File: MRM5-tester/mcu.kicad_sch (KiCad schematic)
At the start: 6 parts, among them U2 STM32L011F4Ux

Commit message: tester PCB 작성중
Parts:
- removed C3: 0.1u, PCM_Capacitor_SMD_AKL:C_0402_1005Metric, symbol PCM_Capacitor_AKL:C_0402
- removed C4: 1u, PCM_Capacitor_SMD_AKL:C_0402_1005Metric, symbol PCM_Capacitor_AKL:C_0402
- removed U2: STM32L011F4Ux, Package_DFN_QFN:ST_UFQFPN-20_3x3mm_P0.5mm, symbol MCU_ST_STM32L0:STM32L011F4Ux
- added D1, D2, D3, D4: LED-WHITE, LED_SMD:LED_0402_1005Metric, symbol Device:LED
- added IC1: STM32G051F8P6, Mouser:SOP65P640X120-20N, symbol ktw07182:STM32G051F8P6
- added Q1, Q2, Q3, Q4: MMBT3906-TP, Mouser:SOT95P237X125-3N, symbol ktw07182:MMBT3906-TP
- added R2, R4, R6, R8: 330, PCM_Resistor_SMD_AKL:R_0402_1005Metric, symbol PCM_Resistor_AKL:R_0402
- added R3, R5, R7: 1k, PCM_Resistor_SMD_AKL:R_0402_1005Metric, symbol PCM_Resistor_AKL:R_0402
- R1: value 10k -> 1k
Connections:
- net 1V6: now also IC1.8 (PA1)
- net GND: now also IC1.5 (VSS/VSSA), R2.2, R4.2, R6.2, R8.2; no longer R1.1
- net MCU_SW_CLK: now also IC1.19 (PA15/PA14-BOOT0)
- net MCU_SW_DIO: now also IC1.18 (PA13)
- net MCU_UART_CTS: now also IC1.16 (PA11[PA9])
- net MCU_UART_RTS: now also IC1.17 (PA12[PA10])
- net MCU_UART_RX: now also IC1.1 (PB7/PB8)
- net MCU_UART_TX: now also IC1.20 (PB3/PB4/PB5/PB6)
- net SYNC_INT: now also IC1.10 (PA3)
- net VDD: now also IC1.4 (VDD/VDDA), Q1.2 (E), Q2.2 (E), Q3.2 (E), Q4.2 (E)
- net at R1.2: now also Q1.1 (B)
- new net: D4.1 (K), R8.1
- new net: D4.2 (A), Q4.3 (C)
- new net: D2.1 (K), R4.1
- new net: D2.2 (A), Q2.3 (C)
- new net: Q2.1 (B), R3.2
- new net: Q3.1 (B), R5.2
- new net: D1.2 (A), Q1.3 (C)
- new net: D3.1 (K), R6.1
- new net: D3.2 (A), Q3.3 (C)
- new net: Q4.1 (B), R7.2
- new net: D1.1 (K), R2.1
- new net 1V6_IFlag: IC1.14 (PA7), R3.1
- new net 1V6_TFlag: IC1.15 (PB0/PB1/PB2/PA8), R1.1
- new net ADC_V: IC1.7 (PA0)
- new net DAC_Z: IC1.11 (PA4)
- new net MCU_NRST: IC1.6 (PF2-NRST)
- new net SUSPEND: IC1.3 (PC15-OSC32_OUT)
- new net WAKEUP: IC1.2 (PB9/PC14-OSC32_IN)
- new net Z_IFlag: IC1.12 (PA5), R7.1
- new net Z_TFlag: IC1.13 (PA6), R5.1
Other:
- moved on the sheet: C1, C2

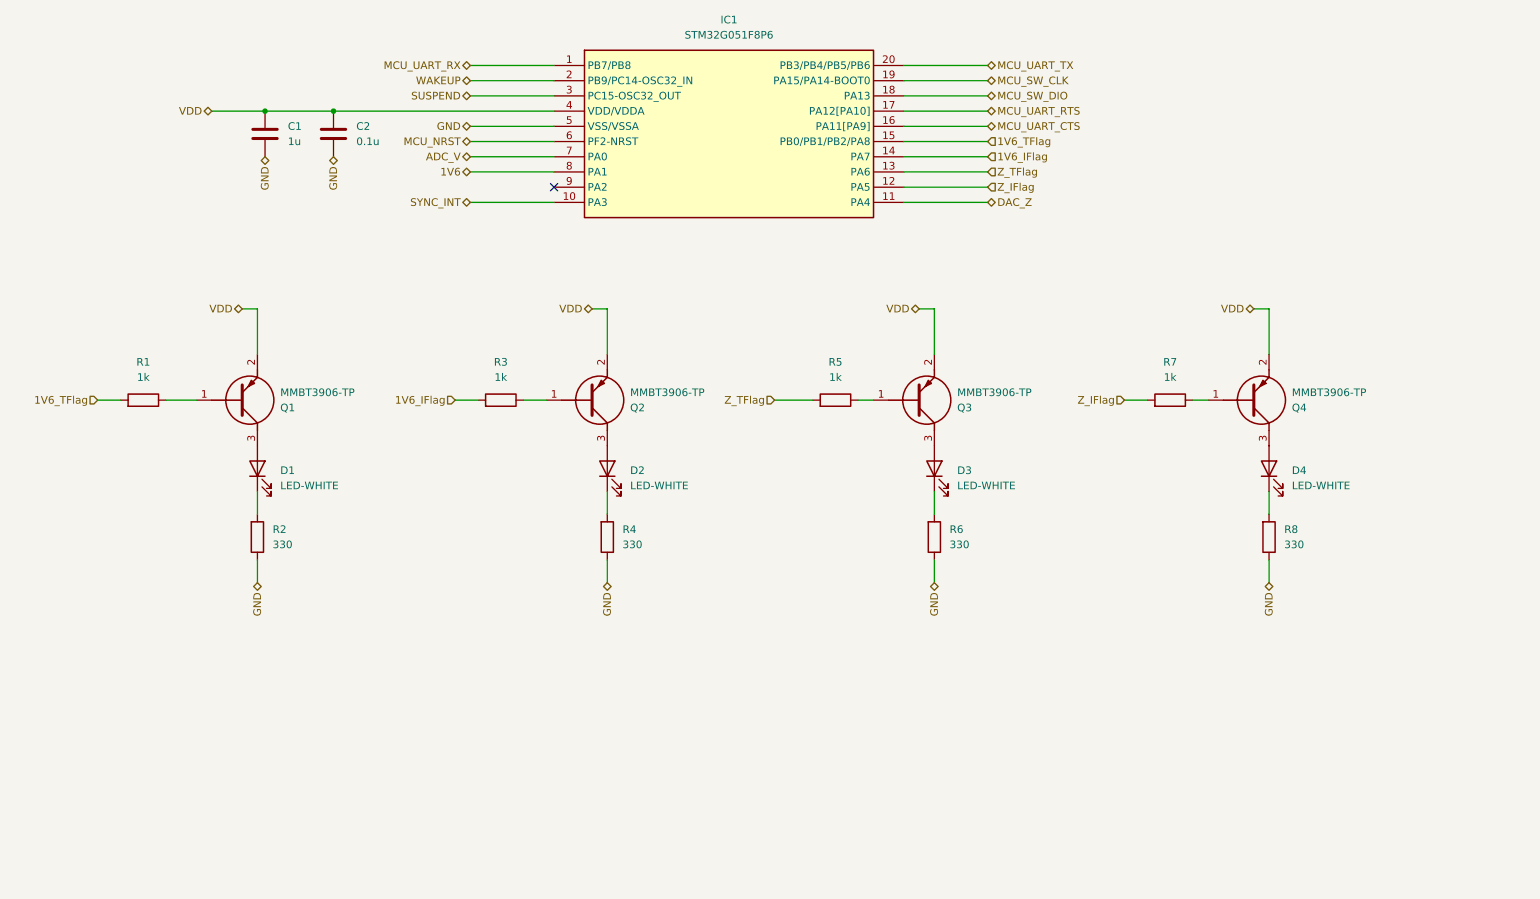
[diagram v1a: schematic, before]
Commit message: tester pcb 디자인 완료
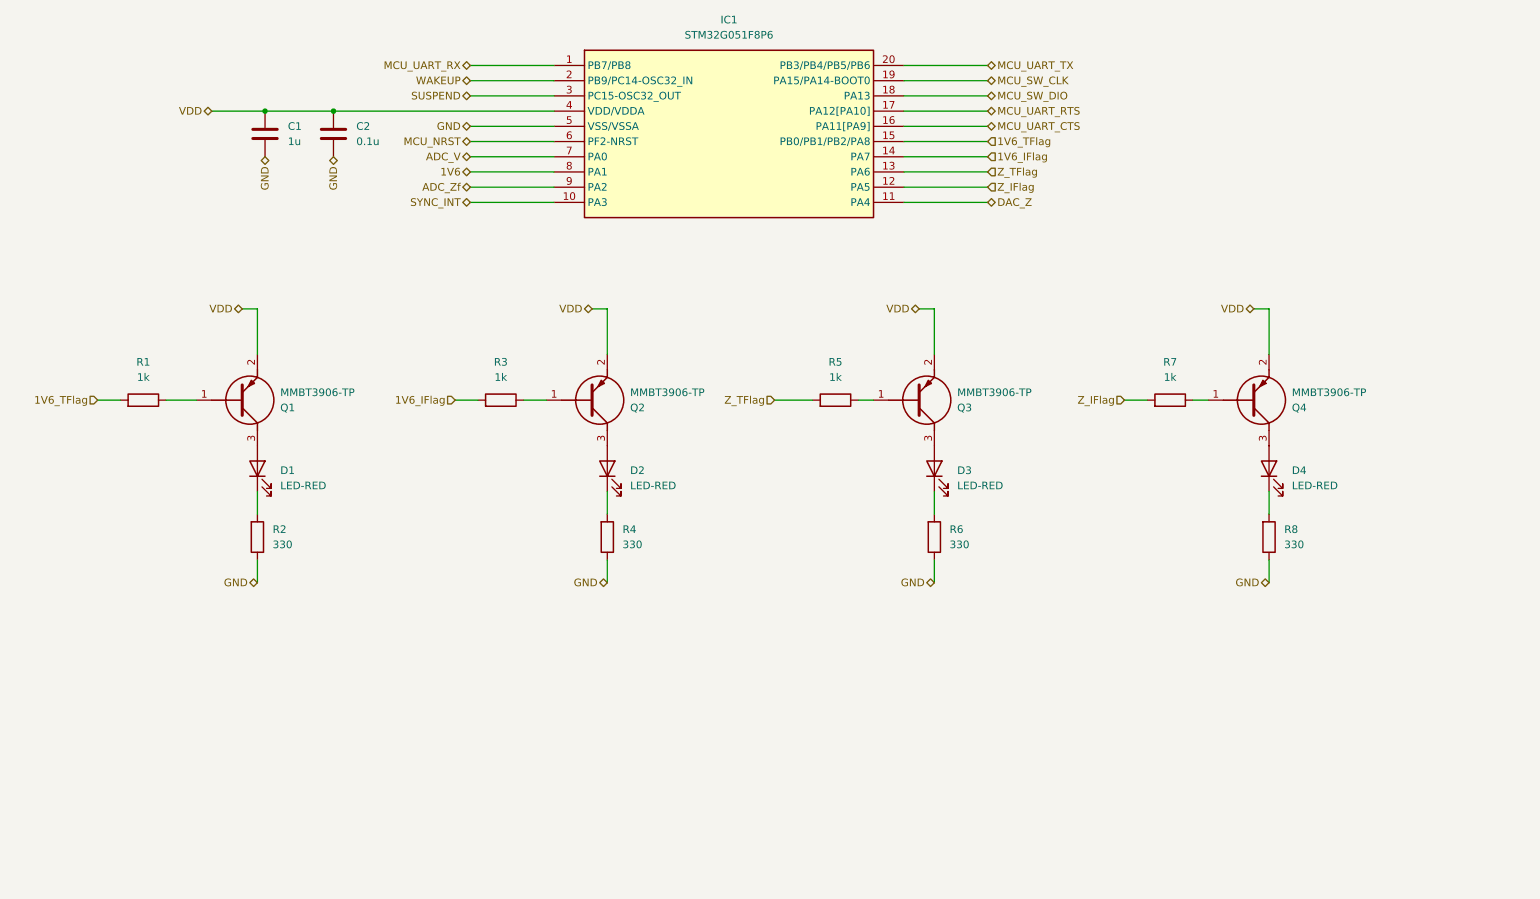
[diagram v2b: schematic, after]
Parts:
- D1, D2, D3, D4: value LED-WHITE -> LED-RED
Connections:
- net ADC_Zf: now reaches IC1.9 (PA2)
- no-connect marks 1 -> 0
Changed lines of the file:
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@@
 		(color 0 0 0 0)
 	)
-	(no_connect
-		(at 119.38 73.66)
-	)
 	(wire
 		(pts
@@
 	(wire
 		(pts
+			(xy 105.41 73.66) (xy 119.38 73.66)
+		)
+		(stroke
+			(width 0)
+			(type default)
+		)
+	)
+	(wire
+		(pts
 			(xy 69.85 93.98) (xy 69.85 101.6)
 		)
@@
 		)
 	)
+	(hierarchical_label "ADC_Zf"
+		(shape bidirectional)
+		(at 105.41 73.66 180)
+		(fields_autoplaced yes)
+		(effects
+			(font
+				(size 1.27 1.27)
+			)
+			(justify right)
+		)
+	)
 	(hierarchical_label "GND"
 		(shape bidirectional)
-		(at 182.88 139.7 270)
+		(at 182.88 139.7 180)
 		(fields_autoplaced yes)
 		(effects
@@
 	(hierarchical_label "GND"
 		(shape bidirectional)
-		(at 69.85 139.7 270)
+		(at 69.85 139.7 180)
 		(fields_autoplaced yes)
 		(effects
@@
 	(hierarchical_label "GND"
 		(shape bidirectional)
-		(at 238.76 139.7 270)
+		(at 238.76 139.7 180)
 		(fields_autoplaced yes)
 		(effects
@@
 	(hierarchical_label "GND"
 		(shape bidirectional)
-		(at 128.27 139.7 270)
+		(at 128.27 139.7 180)
 		(fields_autoplaced yes)
 		(effects
@@
 			)
 		)
-		(property "Value" "LED-WHITE"
+		(property "Value" "LED-RED"
 			(at 242.57 123.5074 90)
 			(effects
@@
 			)
 		)
-		(property "Value" "LED-WHITE"
+		(property "Value" "LED-RED"
 			(at 132.08 123.5074 90)
 			(effects
@@
 			)
 		)
-		(property "Value" "LED-WHITE"
+		(property "Value" "LED-RED"
 			(at 186.69 123.5074 90)
 			(effects
@@
 			)
 		)
-		(property "Value" "LED-WHITE"
+		(property "Value" "LED-RED"
 			(at 73.66 123.5074 90)
 			(effects

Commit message: tester PCB 검토
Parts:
- added Symbol1: ktw07182@gmail.com, Mouser:ktw07182_logo, symbol Mouser:MyLogo
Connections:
- net WAKEUP renamed PUSH_BTN
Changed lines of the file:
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@@
 		)
 	)
-	(hierarchical_label "WAKEUP"
+	(hierarchical_label "PUSH_BTN"
 		(shape bidirectional)
 		(at 105.41 55.88 180)
@@
 					(unit 1)
 				)
+			)
+		)
+	)
+	(symbol
+		(lib_id "Mouser:MyLogo")
+		(at 264.16 161.29 0)
+		(unit 1)
+		(exclude_from_sim no)
+		(in_bom no)
+		(on_board yes)
+		(dnp no)
+		(fields_autoplaced yes)
+		(property "Reference" "Symbol1"
+			(at 264.16 161.29 0)
+			(effects
+				(font
+					(size 1.27 1.27)
+				)
+				(hide yes)
+			)
+		)
+		(property "Value" "ktw07182@gmail.com"
+			(at 263.398 154.94 0)
+			(effects
+				(font
+					(size 1.27 1.27)
+				)
+			)
+		)
+		(property "Footprint" "Mouser:ktw07182_logo"
+			(at 264.16 161.29 0)
+			(effects
+				(font
+					(size 1.27 1.27)
+				)
+				(hide yes)
+			)
+		)
+		(property "Datasheet" ""
+			(at 264.16 161.29 0)
+			(effects
+				(font
+					(size 1.27 1.27)
+				)
+				(hide yes)
+			)
+		)
+		(property "Description" ""
+			(at 264.16 161.29 0)
+			(effects
+				(font
+					(size 1.27 1.27)
+				)
+				(hide yes)
+			)
+		)
+		(instances
+			(project ""
+				(path "/6e775c75-0b09-4e5f-9bff-c5585ac94ad7/02df2b53-e79f-4009-ab3b-419158fe5275"
+					(reference "Symbol1")
+					(unit 1)
+				)

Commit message: MRM5-tester updated
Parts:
- removed D1, D2, D3, D4: LED-RED, LED_SMD:LED_0402_1005Metric, symbol Device:LED
- added LED1, LED2, LED3, LED4: LED_0603_Red, PCM_LED_SMD_AKL:LED_0603_1608Metric, symbol PCM_LED_AKL:LED_0603_Red
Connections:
- net at R8.1: now also LED4.1 (K)
- net at Q4.3 (C): now also LED4.2 (A)
- net at R4.1: now also LED2.1 (K)
- net at Q2.3 (C): now also LED2.2 (A)
- net at Q1.3 (C): now also LED1.2 (A)
- net at R6.1: now also LED3.1 (K)
- net at Q3.3 (C): now also LED3.2 (A)
- net at R2.1: now also LED1.1 (K)

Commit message: case updated
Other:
- moved on the sheet: C1, C2, IC1, LED1, LED2, LED3, LED4, Q1, Q2, Q3, Q4, R1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

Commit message: tester pcb updated
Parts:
- removed LED1, LED2, LED3, LED4: LED_0603_Red, PCM_LED_SMD_AKL:LED_0603_1608Metric, symbol PCM_LED_AKL:LED_0603_Red
- added LED1, LED2, LED3, LED4: LED_5mm, PCM_LED_THT_AKL:LED_D5.0mm, symbol PCM_LED_AKL:LED_5mm
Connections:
- net at Q2.3 (C): now also LED2.2 (A)
- net at R4.1: now also LED2.1 (K)
- net at Q1.3 (C): now also LED1.2 (A)
- net at R2.1: now also LED1.1 (K)
- net at R6.1: now also LED3.1 (K)
- net at Q4.3 (C): now also LED4.2 (A)
- net at Q3.3 (C): now also LED3.2 (A)
- net at R8.1: now also LED4.1 (K)

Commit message: case found!
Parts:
- C1: footprint PCM_Capacitor_SMD_AKL:C_0402_1005Metric -> PCM_Capacitor_SMD_AKL:C_0603_1608Metric
- C2: value 0.1u -> 100n; footprint PCM_Capacitor_SMD_AKL:C_0402_1005Metric -> PCM_Capacitor_SMD_AKL:C_0603_1608Metric
- Q1, Q2, Q3, Q4: value MMBT3906-TP -> SMMBT3906LT3G
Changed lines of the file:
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@@
 			)
 		)
-		(property "Value" "0.1u"
+		(property "Value" "100n"
 			(at 85.09 66.0399 0)
 			(effects
@@
 			)
 		)
-		(property "Footprint" "PCM_Capacitor_SMD_AKL:C_0402_1005Metric"
+		(property "Footprint" "PCM_Capacitor_SMD_AKL:C_0603_1608Metric"
 			(at 80.3148 60.96 0)
 			(effects
@@
 			)
 		)
-		(property "Value" "MMBT3906-TP"
+		(property "Value" "SMMBT3906LT3G"
 			(at 130.81 107.9501 0)
 			(effects
@@
 			)
 		)
-		(property "Value" "MMBT3906-TP"
+		(property "Value" "SMMBT3906LT3G"
 			(at 72.39 107.9501 0)
 			(effects
@@
 			)
 		)
-		(property "Value" "MMBT3906-TP"
+		(property "Value" "SMMBT3906LT3G"
 			(at 241.3 107.9501 0)
 			(effects
@@
 			)
 		)
-		(property "Footprint" "PCM_Capacitor_SMD_AKL:C_0402_1005Metric"
+		(property "Footprint" "PCM_Capacitor_SMD_AKL:C_0603_1608Metric"
 			(at 68.8848 60.96 0)
 			(effects
@@
 			)
 		)
-		(property "Value" "MMBT3906-TP"
+		(property "Value" "SMMBT3906LT3G"
 			(at 185.42 107.9501 0)
 			(effects

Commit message: 케이스에 마춰서 제작 중
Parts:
- LED1, LED2, LED3, LED4: footprint PCM_LED_THT_AKL:LED_D5.0mm -> PCM_LED_SMD_Handsoldering_AKL:LED_1206_3216Metric
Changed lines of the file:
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@@
 			)
 		)
-		(property "Footprint" "PCM_LED_THT_AKL:LED_D5.0mm"
+		(property "Footprint" "PCM_LED_SMD_Handsoldering_AKL:LED_1206_3216Metric"
 			(at 68.58 120.65 0)
 			(effects
@@
 			)
 		)
-		(property "Footprint" "PCM_LED_THT_AKL:LED_D5.0mm"
+		(property "Footprint" "PCM_LED_SMD_Handsoldering_AKL:LED_1206_3216Metric"
 			(at 181.61 120.65 0)
 			(effects
@@
 			)
 		)
-		(property "Footprint" "PCM_LED_THT_AKL:LED_D5.0mm"
+		(property "Footprint" "PCM_LED_SMD_Handsoldering_AKL:LED_1206_3216Metric"
 			(at 127 120.65 0)
 			(effects
@@
 			)
 		)
-		(property "Footprint" "PCM_LED_THT_AKL:LED_D5.0mm"
+		(property "Footprint" "PCM_LED_SMD_Handsoldering_AKL:LED_1206_3216Metric"
 			(at 237.49 120.65 0)
 			(effects
